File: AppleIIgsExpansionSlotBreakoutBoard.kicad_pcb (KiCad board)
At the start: 2 copper layers, 69.1 x 45.7 mm, 5 parts, among them J1 Conn_02x25_Counter_Clockwise, J2 Conn_01x25, J3 Conn_01x25, J4 Conn_01x02, J5 Conn_01x02

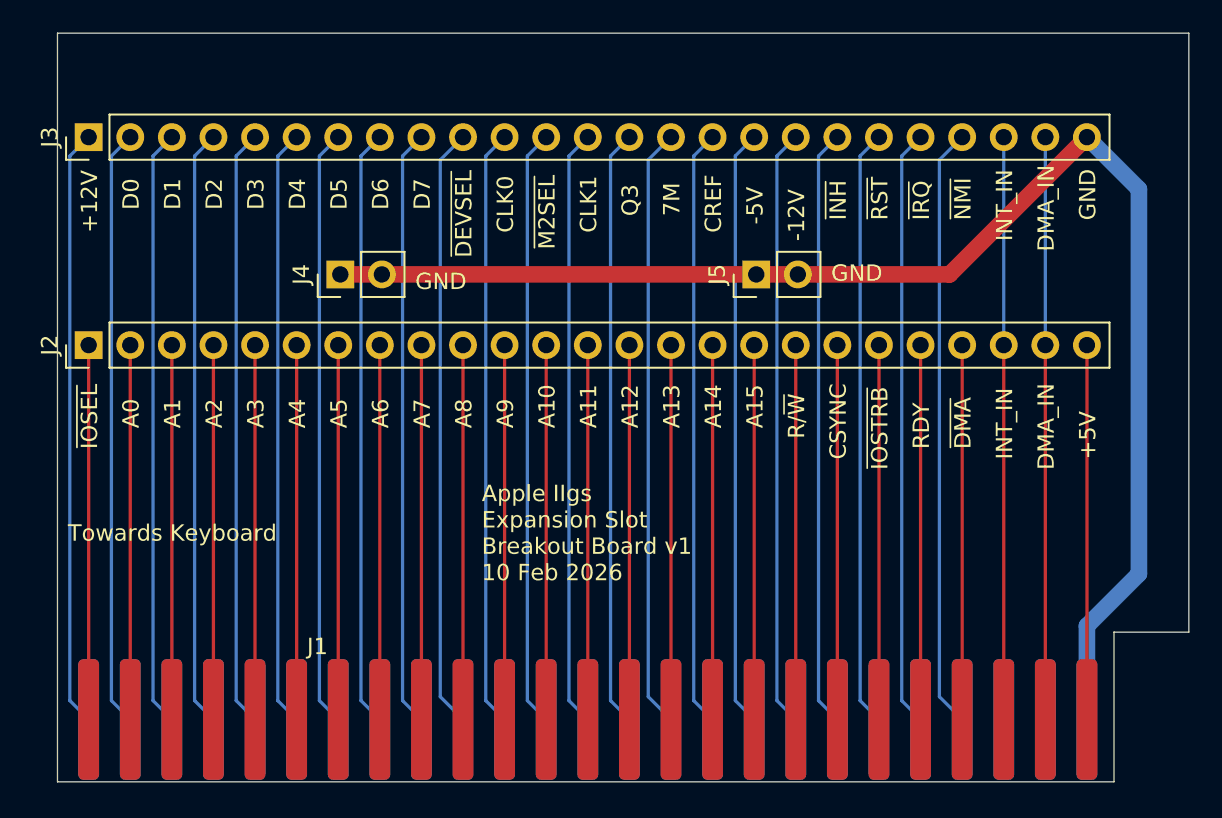
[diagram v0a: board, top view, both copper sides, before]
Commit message: fixed DNA and INT lines not being connected.  cleaned up violations.
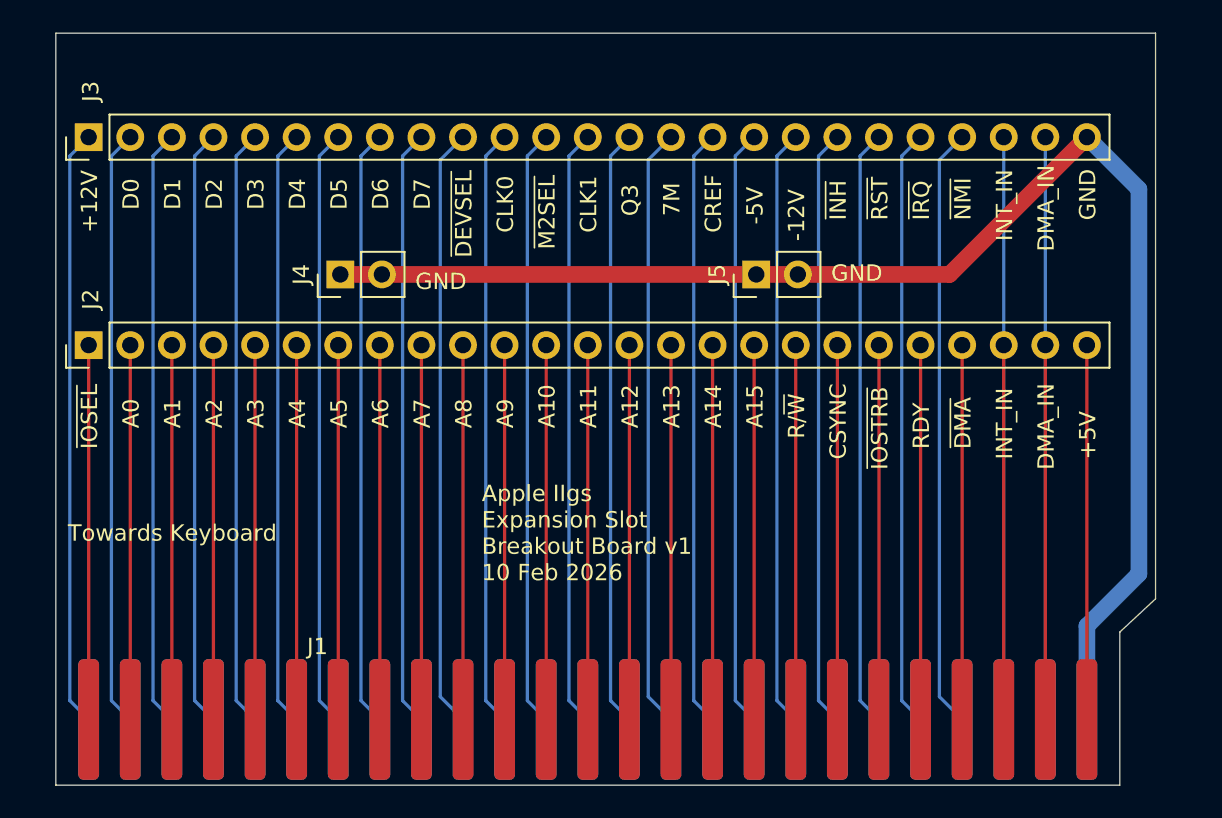
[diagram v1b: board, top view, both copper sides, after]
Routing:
- net /INT_IN: track 35.6 -> 58.4 mm
- net /DMA_IN: track 35.6 -> 58.4 mm
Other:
- board size 69.1 x 45.7 mm -> 67.2 x 45.9 mm
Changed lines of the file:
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@@
 		(tags "Through hole pin header THT 1x25 2.54mm single row")
 		(property "Reference" "J2"
-			(at 0 -2.38 90)
+			(at 2.794 0.127 90)
 			(layer "F.SilkS")
 			(effects
@@
 		(tags "Through hole pin header THT 1x25 2.54mm single row")
 		(property "Reference" "J3"
-			(at 0 -2.38 90)
+			(at 2.794 0.127 90)
 			(layer "F.SilkS")
 			(effects
@@
 	)
 	(gr_line
-		(start 120.396 87.376)
-		(end 124.968 87.376)
+		(start 120.7516 87.376)
+		(end 122.936 85.344)
 		(stroke
 			(width 0.05)
@@
 	)
 	(gr_line
-		(start 124.968 50.8)
-		(end 55.88 50.8)
+		(start 122.936 50.8)
+		(end 55.7784 50.8)
 		(stroke
 			(width 0.05)
@@
 	)
 	(gr_line
-		(start 120.396 96.52)
-		(end 120.396 87.376)
+		(start 120.7516 96.7232)
+		(end 120.7516 87.376)
 		(stroke
 			(width 0.05)
@@
 	)
 	(gr_line
-		(start 55.88 96.52)
-		(end 120.396 96.52)
+		(start 55.7784 96.7232)
+		(end 120.7516 96.7232)
 		(stroke
 			(width 0.05)
@@
 	)
 	(gr_line
-		(start 55.88 50.8)
-		(end 55.88 96.52)
+		(start 55.7784 50.8)
+		(end 55.7784 96.7232)
 		(stroke
 			(width 0.05)
@@
 	)
 	(gr_line
-		(start 124.968 87.376)
-		(end 124.968 50.8)
+		(start 122.936 85.344)
+		(end 122.936 50.8)
 		(stroke
 			(width 0.05)
@@
 	)
 	(segment
+		(start 113.665 92.71)
+		(end 113.665 69.85)
+		(width 0.2)
+		(layer "B.Cu")
+		(net 5)
+	)
+	(segment
 		(start 113.665 69.85)
 		(end 113.665 57.15)
@@
 		(net 9)
 	)
+	(segment
+		(start 116.205 92.71)
+		(end 116.205 69.85)
+		(width 0.2)
+		(layer "B.Cu")
+		(net 9)
+	)
